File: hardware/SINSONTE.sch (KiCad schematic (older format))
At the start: 23 parts, among them J1 BAT, J2 CLOCK, J3 LIGHT_SENSOR, J4 Conn_01x20_Male, J5 Conn_01x20_Male, J9 PROG, Q1 2N7000, Q2 PN2222A, SW1 SW_Push, U1 Pico

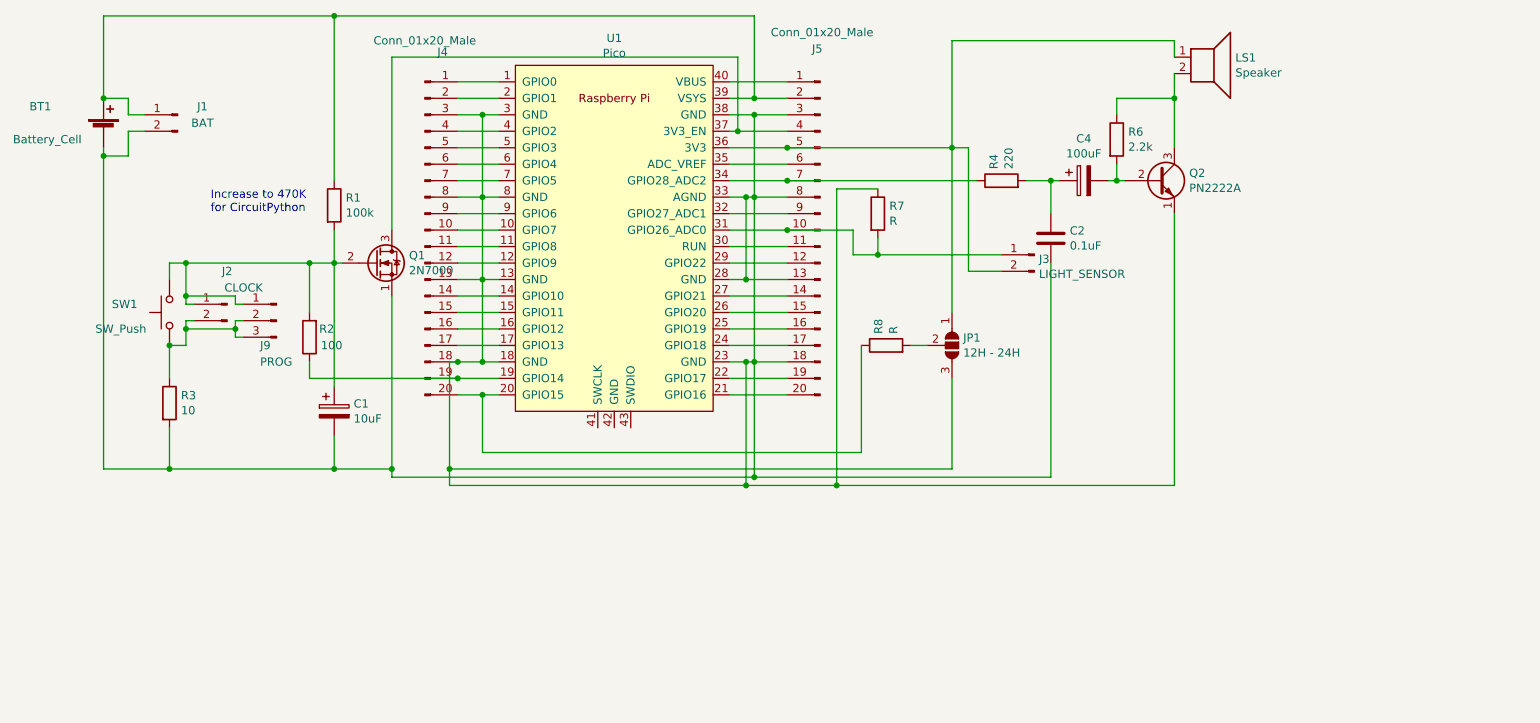
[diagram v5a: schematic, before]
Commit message: added proto area
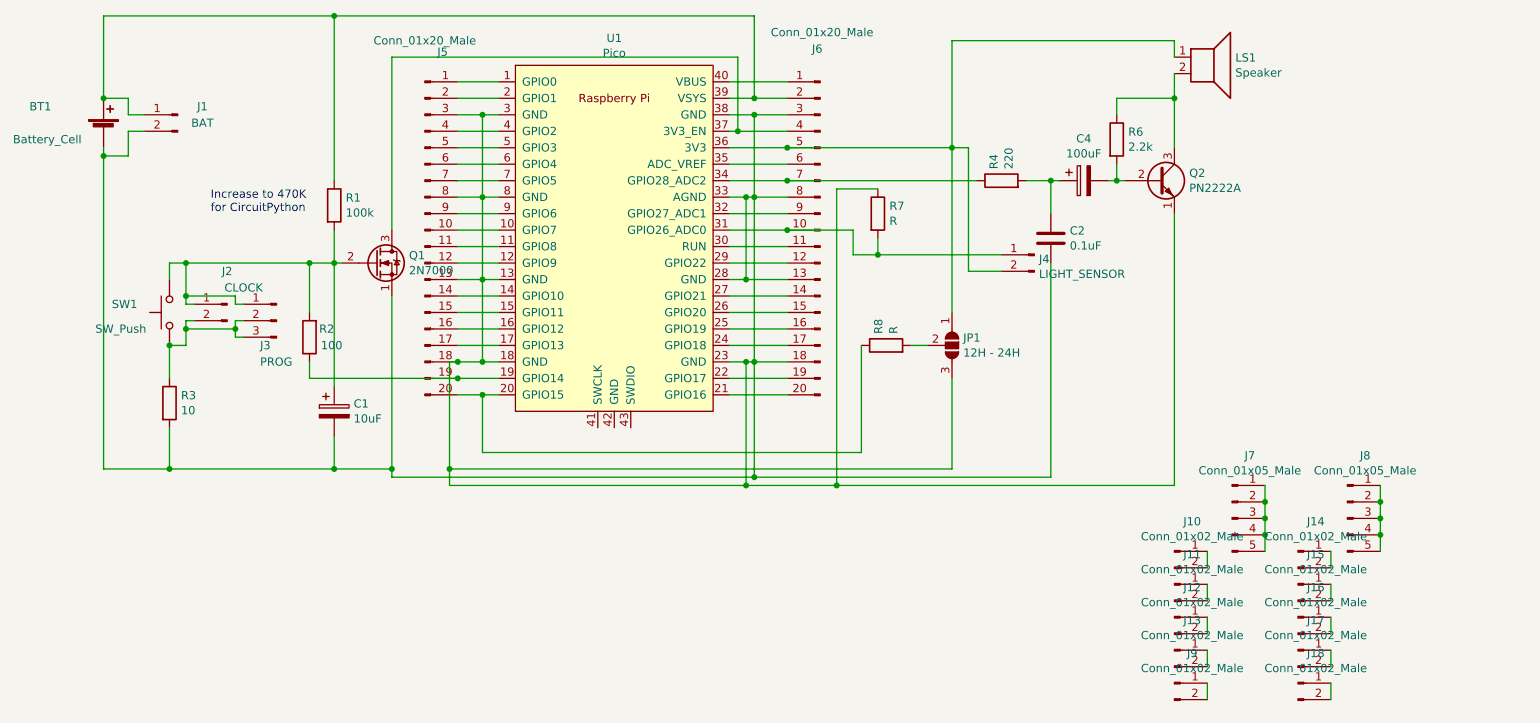
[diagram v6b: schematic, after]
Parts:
- added J10, J11, J12, J13, J14, J15, J16, J17, J18, J9: Conn_01x02_Male, Connector_PinHeader_2.54mm:PinHeader_1x02_P2.54mm_Vertical, symbol Connector:Conn_01x02_Male
- added J7, J8: Conn_01x05_Male, Connector_PinHeader_2.54mm:PinHeader_1x05_P2.54mm_Vertical, symbol Connector:Conn_01x05_Male
- renumbered J9 to J3, J3 to J4, J4 to J5, J5 to J6
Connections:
- new net: J8.1 (Pin_1), J8.2 (Pin_2), J8.3 (Pin_3), J8.4 (Pin_4), J8.5 (Pin_5)
- new net: J7.1 (Pin_1), J7.2 (Pin_2), J7.3 (Pin_3), J7.4 (Pin_4), J7.5 (Pin_5)
- new net: J9.1 (Pin_1), J9.2 (Pin_2)
- new net: J13.1 (Pin_1), J13.2 (Pin_2)
- new net: J12.1 (Pin_1), J12.2 (Pin_2)
- new net: J11.1 (Pin_1), J11.2 (Pin_2)
- new net: J10.1 (Pin_1), J10.2 (Pin_2)
- new net: J18.1 (Pin_1), J18.2 (Pin_2)
- new net: J17.1 (Pin_1), J17.2 (Pin_2)
- new net: J16.1 (Pin_1), J16.2 (Pin_2)
- new net: J15.1 (Pin_1), J15.2 (Pin_2)
- new net: J14.1 (Pin_1), J14.2 (Pin_2)
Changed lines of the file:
@@
 	9000 2950 9000 2650
 $Comp
-L Connector:Conn_01x02_Male J3
+L Connector:Conn_01x02_Male J4
 U 1 1 6047B078
 P 8150 3600
-F 0 "J3" H 8122 3574 50  0000 R CNN
+F 0 "J4" H 8122 3574 50  0000 R CNN
 F 1 "LIGHT_SENSOR" H 8122 3483 50  0000 R CNN
 F 2 "Connector_PinHeader_2.54mm:PinHeader_1x02_P2.54mm_Vertical" H 8150 3600 50  0001 C CNN
@@
 	6450 2750 6450 3250
 $Comp
-L Connector:Conn_01x03_Male J9
+L Connector:Conn_01x03_Male J3
 U 1 1 60882A91
 P 3550 4000
-F 0 "J9" H 3650 3850 50  0000 R CNN
+F 0 "J3" H 3650 3850 50  0000 R CNN
 F 1 "PROG" H 3650 3750 50  0000 R CNN
 F 2 "Connector_PinHeader_2.54mm:PinHeader_1x03_P2.54mm_Vertical" H 3550 4000 50  0001 C CNN
@@
 	4600 4250 4650 4250
 $Comp
-L Connector:Conn_01x20_Male J4
+L Connector:Conn_01x20_Male J5
 U 1 1 618AE8C2
 P 4450 3450
-F 0 "J4" H 4558 4531 50  0000 C CNN
+F 0 "J5" H 4558 4531 50  0000 C CNN
 F 1 "Conn_01x20_Male" H 4450 4600 50  0000 C CNN
 F 2 "Connector_PinHeader_2.54mm:PinHeader_1x20_P2.54mm_Vertical" H 4450 3450 50  0001 C CNN
@@
 Connection ~ 6650 3450
 $Comp
-L Connector:Conn_01x20_Male J5
+L Connector:Conn_01x20_Male J6
 U 1 1 618B0A3E
 P 6850 3450
-F 0 "J5" H 6900 4550 50  0000 R CNN
+F 0 "J6" H 6900 4550 50  0000 R CNN
 F 1 "Conn_01x20_Male" H 7150 4650 50  0000 R CNN
 F 2 "Connector_PinHeader_2.54mm:PinHeader_1x20_P2.54mm_Vertical" H 6850 3450 50  0001 C CNN
@@
 	6350 2850 6650 2850
 Connection ~ 6350 2850
+$Comp
+L Connector:Conn_01x05_Male J8
+U 1 1 61902046
+P 10050 5200
+F 0 "J8" H 10158 5581 50  0000 C CNN
+F 1 "Conn_01x05_Male" H 10158 5490 50  0000 C CNN
+F 2 "Connector_PinHeader_2.54mm:PinHeader_1x05_P2.54mm_Vertical" H 10050 5200 50  0001 C CNN
+F 3 "~" H 10050 5200 50  0001 C CNN
+	1    10050 5200
+	1    0    0    -1
+$EndComp
+$Comp
+L Connector:Conn_01x05_Male J7
+U 1 1 6190E2F0
+P 9350 5200
+F 0 "J7" H 9458 5581 50  0000 C CNN
+F 1 "Conn_01x05_Male" H 9458 5490 50  0000 C CNN
+F 2 "Connector_PinHeader_2.54mm:PinHeader_1x05_P2.54mm_Vertical" H 9350 5200 50  0001 C CNN
+F 3 "~" H 9350 5200 50  0001 C CNN
+	1    9350 5200
+	1    0    0    -1
+$EndComp
+Wire Wire Line
+	9550 5000 9550 5100
+Wire Wire Line
+	9550 5200 9550 5100
+Connection ~ 9550 5100
+Wire Wire Line
+	9550 5300 9550 5200
+Connection ~ 9550 5200
+Wire Wire Line
+	9550 5400 9550 5300
+Connection ~ 9550 5300
+Wire Wire Line
+	10250 5400 10250 5300
+Wire Wire Line
+	10250 5300 10250 5200
+Connection ~ 10250 5300
+Wire Wire Line
+	10250 5100 10250 5000
+Wire Wire Line
+	10250 5200 10250 5100
+Connection ~ 10250 5200
+Connection ~ 10250 5100
+$Comp
+L Connector:Conn_01x02_Male J9
+U 1 1 6194F5CD
+P 9000 6200
+F 0 "J9" H 9108 6381 50  0000 C CNN
+F 1 "Conn_01x02_Male" H 9108 6290 50  0000 C CNN
+F 2 "Connector_PinHeader_2.54mm:PinHeader_1x02_P2.54mm_Vertical" H 9000 6200 50  0001 C CNN
+F 3 "~" H 9000 6200 50  0001 C CNN
+	1    9000 6200
+	1    0    0    -1
+$EndComp
+Wire Wire Line
+	9200 6200 9200 6300
+$Comp
+L Connector:Conn_01x02_Male J13
+U 1 1 6195EF97
+P 9000 6000
+F 0 "J13" H 9108 6181 50  0000 C CNN
+F 1 "Conn_01x02_Male" H 9108 6090 50  0000 C CNN
+F 2 "Connector_PinHeader_2.54mm:PinHeader_1x02_P2.54mm_Vertical" H 9000 6000 50  0001 C CNN
+F 3 "~" H 9000 6000 50  0001 C CNN
+	1    9000 6000
+	1    0    0    -1
+$EndComp
+$Comp
+L Connector:Conn_01x02_Male J12
+U 1 1 6195FB17
+P 9000 5800
+F 0 "J12" H 9108 5981 50  0000 C CNN
+F 1 "Conn_01x02_Male" H 9108 5890 50  0000 C CNN
+F 2 "Connector_PinHeader_2.54mm:PinHeader_1x02_P2.54mm_Vertical" H 9000 5800 50  0001 C CNN
+F 3 "~" H 9000 5800 50  0001 C CNN
+	1    9000 5800
+	1    0    0    -1
+$EndComp
+$Comp
+L Connector:Conn_01x02_Male J11
+U 1 1 6196008A
+P 9000 5600
+F 0 "J11" H 9108 5781 50  0000 C CNN
+F 1 "Conn_01x02_Male" H 9108 5690 50  0000 C CNN
+F 2 "Connector_PinHeader_2.54mm:PinHeader_1x02_P2.54mm_Vertical" H 9000 5600 50  0001 C CNN
+F 3 "~" H 9000 5600 50  0001 C CNN
+	1    9000 5600
+	1    0    0    -1
+$EndComp
+$Comp
+L Connector:Conn_01x02_Male J10
+U 1 1 61960476
+P 9000 5400
+F 0 "J10" H 9108 5581 50  0000 C CNN
+F 1 "Conn_01x02_Male" H 9108 5490 50  0000 C CNN
+F 2 "Connector_PinHeader_2.54mm:PinHeader_1x02_P2.54mm_Vertical" H 9000 5400 50  0001 C CNN
+F 3 "~" H 9000 5400 50  0001 C CNN
+	1    9000 5400
+	1    0    0    -1
+$EndComp
+Wire Wire Line
+	9200 6000 9200 6100
+Wire Wire Line
+	9200 5900 9200 5800
+Wire Wire Line
+	9200 5700 9200 5600
+Wire Wire Line
+	9200 5500 9200 5400
+$Comp
+L Connector:Conn_01x02_Male J18
+U 1 1 61984084
+P 9750 6200
+F 0 "J18" H 9858 6381 50  0000 C CNN
+F 1 "Conn_01x02_Male" H 9858 6290 50  0000 C CNN
+F 2 "Connector_PinHeader_2.54mm:PinHeader_1x02_P2.54mm_Vertical" H 9750 6200 50  0001 C CNN
+F 3 "~" H 9750 6200 50  0001 C CNN
+	1    9750 6200
+	1    0    0    -1
+$EndComp
+$Comp
+L Connector:Conn_01x02_Male J17
+U 1 1 61984FA8
+P 9750 6000
+F 0 "J17" H 9858 6181 50  0000 C CNN
+F 1 "Conn_01x02_Male" H 9858 6090 50  0000 C CNN
+F 2 "Connector_PinHeader_2.54mm:PinHeader_1x02_P2.54mm_Vertical" H 9750 6000 50  0001 C CNN
+F 3 "~" H 9750 6000 50  0001 C CNN
+	1    9750 6000
+	1    0    0    -1
+$EndComp
+$Comp
+L Connector:Conn_01x02_Male J16
+U 1 1 61985BD2
+P 9750 5800
+F 0 "J16" H 9858 5981 50  0000 C CNN
+F 1 "Conn_01x02_Male" H 9858 5890 50  0000 C CNN
+F 2 "Connector_PinHeader_2.54mm:PinHeader_1x02_P2.54mm_Vertical" H 9750 5800 50  0001 C CNN
+F 3 "~" H 9750 5800 50  0001 C CNN
+	1    9750 5800
+	1    0    0    -1
+$EndComp
+$Comp
+L Connector:Conn_01x02_Male J15
+U 1 1 61986D11
+P 9750 5600
+F 0 "J15" H 9858 5781 50  0000 C CNN
+F 1 "Conn_01x02_Male" H 9858 5690 50  0000 C CNN
+F 2 "Connector_PinHeader_2.54mm:PinHeader_1x02_P2.54mm_Vertical" H 9750 5600 50  0001 C CNN
+F 3 "~" H 9750 5600 50  0001 C CNN
+	1    9750 5600
+	1    0    0    -1
+$EndComp
+$Comp
+L Connector:Conn_01x02_Male J14
+U 1 1 619876D5
+P 9750 5400
+F 0 "J14" H 9858 5581 50  0000 C CNN
+F 1 "Conn_01x02_Male" H 9858 5490 50  0000 C CNN
+F 2 "Connector_PinHeader_2.54mm:PinHeader_1x02_P2.54mm_Vertical" H 9750 5400 50  0001 C CNN
+F 3 "~" H 9750 5400 50  0001 C CNN
+	1    9750 5400
+	1    0    0    -1
+$EndComp
+Wire Wire Line
+	9950 5400 9950 5500
+Wire Wire Line
+	9950 5600 9950 5700
+Wire Wire Line
+	9950 5800 9950 5900
+Wire Wire Line
+	9950 6000 9950 6100
+Wire Wire Line
+	9950 6200 9950 6300
 $EndSCHEMATC

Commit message: minor adjustments
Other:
- note added: "PROTO AREA"
- moved on the sheet: J10, J11, J12, J13, J14, J15, J16, J17, J18, J7, J8, J9
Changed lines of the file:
@@
 L Connector:Conn_01x05_Male J8
 U 1 1 61902046
-P 10050 5200
-F 0 "J8" H 10158 5581 50  0000 C CNN
-F 1 "Conn_01x05_Male" H 10158 5490 50  0000 C CNN
-F 2 "Connector_PinHeader_2.54mm:PinHeader_1x05_P2.54mm_Vertical" H 10050 5200 50  0001 C CNN
-F 3 "~" H 10050 5200 50  0001 C CNN
-	1    10050 5200
+P 10650 5650
+F 0 "J8" H 10758 6031 50  0000 C CNN
+F 1 "Conn_01x05_Male" H 10758 5940 50  0000 C CNN
+F 2 "Connector_PinHeader_2.54mm:PinHeader_1x05_P2.54mm_Vertical" H 10650 5650 50  0001 C CNN
+F 3 "~" H 10650 5650 50  0001 C CNN
+	1    10650 5650
 	1    0    0    -1
 $EndComp
@@
 L Connector:Conn_01x05_Male J7
 U 1 1 6190E2F0
-P 9350 5200
-F 0 "J7" H 9458 5581 50  0000 C CNN
-F 1 "Conn_01x05_Male" H 9458 5490 50  0000 C CNN
-F 2 "Connector_PinHeader_2.54mm:PinHeader_1x05_P2.54mm_Vertical" H 9350 5200 50  0001 C CNN
-F 3 "~" H 9350 5200 50  0001 C CNN
-	1    9350 5200
+P 9600 5650
+F 0 "J7" H 9708 6031 50  0000 C CNN
+F 1 "Conn_01x05_Male" H 9708 5940 50  0000 C CNN
+F 2 "Connector_PinHeader_2.54mm:PinHeader_1x05_P2.54mm_Vertical" H 9600 5650 50  0001 C CNN
+F 3 "~" H 9600 5650 50  0001 C CNN
+	1    9600 5650
 	1    0    0    -1
 $EndComp
 Wire Wire Line
-	9550 5000 9550 5100
+	9800 5450 9800 5550
 Wire Wire Line
-	9550 5200 9550 5100
-Connection ~ 9550 5100
+	9800 5650 9800 5550
+Connection ~ 9800 5550
 Wire Wire Line
-	9550 5300 9550 5200
-Connection ~ 9550 5200
+	9800 5750 9800 5650
+Connection ~ 9800 5650
 Wire Wire Line
-	9550 5400 9550 5300
-Connection ~ 9550 5300
+	9800 5850 9800 5750
+Connection ~ 9800 5750
 Wire Wire Line
-	10250 5400 10250 5300
+	10850 5850 10850 5750
 Wire Wire Line
-	10250 5300 10250 5200
-Connection ~ 10250 5300
+	10850 5750 10850 5650
+Connection ~ 10850 5750
 Wire Wire Line
-	10250 5100 10250 5000
+	10850 5550 10850 5450
 Wire Wire Line
-	10250 5200 10250 5100
-Connection ~ 10250 5200
-Connection ~ 10250 5100
+	10850 5650 10850 5550
+Connection ~ 10850 5650
+Connection ~ 10850 5550
 $Comp
 L Connector:Conn_01x02_Male J9
 U 1 1 6194F5CD
-P 9000 6200
-F 0 "J9" H 9108 6381 50  0000 C CNN
-F 1 "Conn_01x02_Male" H 9108 6290 50  0000 C CNN
-F 2 "Connector_PinHeader_2.54mm:PinHeader_1x02_P2.54mm_Vertical" H 9000 6200 50  0001 C CNN
-F 3 "~" H 9000 6200 50  0001 C CNN
-	1    9000 6200
+P 9100 6250
+F 0 "J9" H 9208 6431 50  0000 C CNN
+F 1 "Conn_01x02_Male" H 9208 6340 50  0000 C CNN
+F 2 "Connector_PinHeader_2.54mm:PinHeader_1x02_P2.54mm_Vertical" H 9100 6250 50  0001 C CNN
+F 3 "~" H 9100 6250 50  0001 C CNN
+	1    9100 6250
 	1    0    0    -1
 $EndComp
 Wire Wire Line
-	9200 6200 9200 6300
+	9300 6250 9300 6350
 $Comp
 L Connector:Conn_01x02_Male J13
 U 1 1 6195EF97
-P 9000 6000
-F 0 "J13" H 9108 6181 50  0000 C CNN
-F 1 "Conn_01x02_Male" H 9108 6090 50  0000 C CNN
-F 2 "Connector_PinHeader_2.54mm:PinHeader_1x02_P2.54mm_Vertical" H 9000 6000 50  0001 C CNN
-F 3 "~" H 9000 6000 50  0001 C CNN
-	1    9000 6000
+P 9100 6050
+F 0 "J13" H 9208 6231 50  0000 C CNN
+F 1 "Conn_01x02_Male" H 9208 6140 50  0000 C CNN
+F 2 "Connector_PinHeader_2.54mm:PinHeader_1x02_P2.54mm_Vertical" H 9100 6050 50  0001 C CNN
+F 3 "~" H 9100 6050 50  0001 C CNN
+	1    9100 6050
 	1    0    0    -1
 $EndComp
@@
 L Connector:Conn_01x02_Male J12
 U 1 1 6195FB17
-P 9000 5800
-F 0 "J12" H 9108 5981 50  0000 C CNN
-F 1 "Conn_01x02_Male" H 9108 5890 50  0000 C CNN
-F 2 "Connector_PinHeader_2.54mm:PinHeader_1x02_P2.54mm_Vertical" H 9000 5800 50  0001 C CNN
-F 3 "~" H 9000 5800 50  0001 C CNN
-	1    9000 5800
+P 9100 5850
+F 0 "J12" H 9208 6031 50  0000 C CNN
+F 1 "Conn_01x02_Male" H 9208 5940 50  0000 C CNN
+F 2 "Connector_PinHeader_2.54mm:PinHeader_1x02_P2.54mm_Vertical" H 9100 5850 50  0001 C CNN
+F 3 "~" H 9100 5850 50  0001 C CNN
+	1    9100 5850
 	1    0    0    -1
 $EndComp
@@
 L Connector:Conn_01x02_Male J11
 U 1 1 6196008A
-P 9000 5600
-F 0 "J11" H 9108 5781 50  0000 C CNN
-F 1 "Conn_01x02_Male" H 9108 5690 50  0000 C CNN
-F 2 "Connector_PinHeader_2.54mm:PinHeader_1x02_P2.54mm_Vertical" H 9000 5600 50  0001 C CNN
-F 3 "~" H 9000 5600 50  0001 C CNN
-	1    9000 5600
+P 9100 5650
+F 0 "J11" H 9208 5831 50  0000 C CNN
+F 1 "Conn_01x02_Male" H 9208 5740 50  0000 C CNN
+F 2 "Connector_PinHeader_2.54mm:PinHeader_1x02_P2.54mm_Vertical" H 9100 5650 50  0001 C CNN
+F 3 "~" H 9100 5650 50  0001 C CNN
+	1    9100 5650
 	1    0    0    -1
 $EndComp
@@
 L Connector:Conn_01x02_Male J10
 U 1 1 61960476
-P 9000 5400
-F 0 "J10" H 9108 5581 50  0000 C CNN
-F 1 "Conn_01x02_Male" H 9108 5490 50  0000 C CNN
-F 2 "Connector_PinHeader_2.54mm:PinHeader_1x02_P2.54mm_Vertical" H 9000 5400 50  0001 C CNN
-F 3 "~" H 9000 5400 50  0001 C CNN
-	1    9000 5400
+P 9100 5450
+F 0 "J10" H 9208 5631 50  0000 C CNN
+F 1 "Conn_01x02_Male" H 9208 5540 50  0000 C CNN
+F 2 "Connector_PinHeader_2.54mm:PinHeader_1x02_P2.54mm_Vertical" H 9100 5450 50  0001 C CNN
+F 3 "~" H 9100 5450 50  0001 C CNN
+	1    9100 5450
 	1    0    0    -1
 $EndComp
 Wire Wire Line
-	9200 6000 9200 6100
+	9300 6050 9300 6150
 Wire Wire Line
-	9200 5900 9200 5800
+	9300 5950 9300 5850
 Wire Wire Line
-	9200 5700 9200 5600
+	9300 5750 9300 5650
 Wire Wire Line
-	9200 5500 9200 5400
+	9300 5550 9300 5450
 $Comp
 L Connector:Conn_01x02_Male J18
 U 1 1 61984084
-P 9750 6200
-F 0 "J18" H 9858 6381 50  0000 C CNN
-F 1 "Conn_01x02_Male" H 9858 6290 50  0000 C CNN
-F 2 "Connector_PinHeader_2.54mm:PinHeader_1x02_P2.54mm_Vertical" H 9750 6200 50  0001 C CNN
-F 3 "~" H 9750 6200 50  0001 C CNN
-	1    9750 6200
+P 10050 6250
+F 0 "J18" H 10158 6431 50  0000 C CNN
+F 1 "Conn_01x02_Male" H 10158 6340 50  0000 C CNN
+F 2 "Connector_PinHeader_2.54mm:PinHeader_1x02_P2.54mm_Vertical" H 10050 6250 50  0001 C CNN
+F 3 "~" H 10050 6250 50  0001 C CNN
+	1    10050 6250
 	1    0    0    -1
 $EndComp
@@
 L Connector:Conn_01x02_Male J17
 U 1 1 61984FA8
-P 9750 6000
-F 0 "J17" H 9858 6181 50  0000 C CNN
-F 1 "Conn_01x02_Male" H 9858 6090 50  0000 C CNN
-F 2 "Connector_PinHeader_2.54mm:PinHeader_1x02_P2.54mm_Vertical" H 9750 6000 50  0001 C CNN
-F 3 "~" H 9750 6000 50  0001 C CNN
-	1    9750 6000
+P 10050 6050
+F 0 "J17" H 10158 6231 50  0000 C CNN
+F 1 "Conn_01x02_Male" H 10158 6140 50  0000 C CNN
+F 2 "Connector_PinHeader_2.54mm:PinHeader_1x02_P2.54mm_Vertical" H 10050 6050 50  0001 C CNN
+F 3 "~" H 10050 6050 50  0001 C CNN
+	1    10050 6050
 	1    0    0    -1
 $EndComp
@@
 L Connector:Conn_01x02_Male J16
 U 1 1 61985BD2
-P 9750 5800
-F 0 "J16" H 9858 5981 50  0000 C CNN
-F 1 "Conn_01x02_Male" H 9858 5890 50  0000 C CNN
-F 2 "Connector_PinHeader_2.54mm:PinHeader_1x02_P2.54mm_Vertical" H 9750 5800 50  0001 C CNN
-F 3 "~" H 9750 5800 50  0001 C CNN
-	1    9750 5800
+P 10050 5850
+F 0 "J16" H 10158 6031 50  0000 C CNN
+F 1 "Conn_01x02_Male" H 10158 5940 50  0000 C CNN
+F 2 "Connector_PinHeader_2.54mm:PinHeader_1x02_P2.54mm_Vertical" H 10050 5850 50  0001 C CNN
+F 3 "~" H 10050 5850 50  0001 C CNN
+	1    10050 5850
 	1    0    0    -1
 $EndComp
@@
 L Connector:Conn_01x02_Male J15
 U 1 1 61986D11
-P 9750 5600
-F 0 "J15" H 9858 5781 50  0000 C CNN
-F 1 "Conn_01x02_Male" H 9858 5690 50  0000 C CNN
-F 2 "Connector_PinHeader_2.54mm:PinHeader_1x02_P2.54mm_Vertical" H 9750 5600 50  0001 C CNN
-F 3 "~" H 9750 5600 50  0001 C CNN
-	1    9750 5600
+P 10050 5650
+F 0 "J15" H 10158 5831 50  0000 C CNN
+F 1 "Conn_01x02_Male" H 10158 5740 50  0000 C CNN
+F 2 "Connector_PinHeader_2.54mm:PinHeader_1x02_P2.54mm_Vertical" H 10050 5650 50  0001 C CNN
+F 3 "~" H 10050 5650 50  0001 C CNN
+	1    10050 5650
 	1    0    0    -1
 $EndComp
@@
 L Connector:Conn_01x02_Male J14
 U 1 1 619876D5
-P 9750 5400
-F 0 "J14" H 9858 5581 50  0000 C CNN
-F 1 "Conn_01x02_Male" H 9858 5490 50  0000 C CNN
-F 2 "Connector_PinHeader_2.54mm:PinHeader_1x02_P2.54mm_Vertical" H 9750 5400 50  0001 C CNN
-F 3 "~" H 9750 5400 50  0001 C CNN
-	1    9750 5400
+P 10050 5450
+F 0 "J14" H 10158 5631 50  0000 C CNN
+F 1 "Conn_01x02_Male" H 10158 5540 50  0000 C CNN
+F 2 "Connector_PinHeader_2.54mm:PinHeader_1x02_P2.54mm_Vertical" H 10050 5450 50  0001 C CNN
+F 3 "~" H 10050 5450 50  0001 C CNN
+	1    10050 5450
 	1    0    0    -1
 $EndComp
 Wire Wire Line
-	9950 5400 9950 5500
+	10250 5450 10250 5550
 Wire Wire Line
-	9950 5600 9950 5700
+	10250 5650 10250 5750
 Wire Wire Line
-	9950 5800 9950 5900
+	10250 5850 10250 5950
 Wire Wire Line
-	9950 6000 9950 6100
+	10250 6050 10250 6150
 Wire Wire Line
-	9950 6200 9950 6300
+	10250 6250 10250 6350
+Text Notes 9750 5150 0    50   ~ 0
+PROTO AREA
 $EndSCHEMATC
